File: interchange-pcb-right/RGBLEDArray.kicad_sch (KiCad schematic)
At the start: 60 parts

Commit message: feat(right): add LCSC part numbers to schematics
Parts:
- C1, C10, C11, C12, C13, C14, C15, C16, C17, C18, C19, C2, C20, C21, C22, C23, C24, C25, C26, C27, C28, C29, C3, C30, C4, C5, C6, C7, C8, C9: LCSC (none) -> C14663
- LED1, LED10, LED11, LED12, LED13, LED14, LED15, LED16, LED17, LED18, LED19, LED2, LED20, LED21, LED22, LED23, LED24, LED25, LED26, LED27, LED28, LED29, LED3, LED30, LED4, LED5, LED6, LED7, LED8, LED9: LCSC (none) -> C5149201

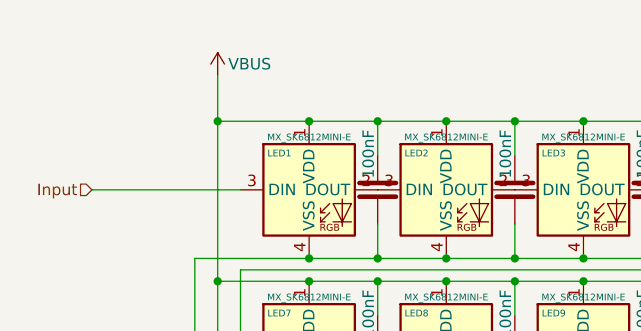
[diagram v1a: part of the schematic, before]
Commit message: wip: add reverse polarity protection and fix buzzer
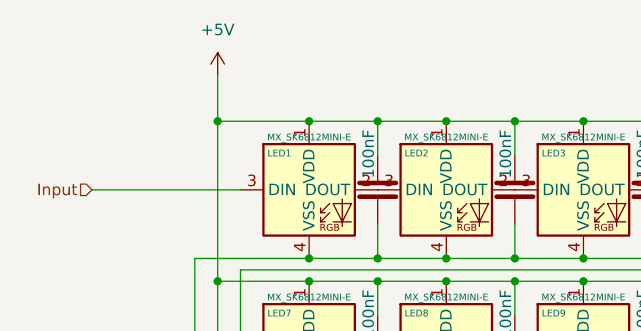
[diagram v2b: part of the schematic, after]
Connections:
- net VBUS renamed +5V
